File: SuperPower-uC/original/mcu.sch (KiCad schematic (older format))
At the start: 41 parts, among them J4 mcu_pinout, J5 mcu_pinout, Q5 S8050, Q6 S8050, U4 CP2102N-A01-GQFN28, U5 ESP32-WROOM32

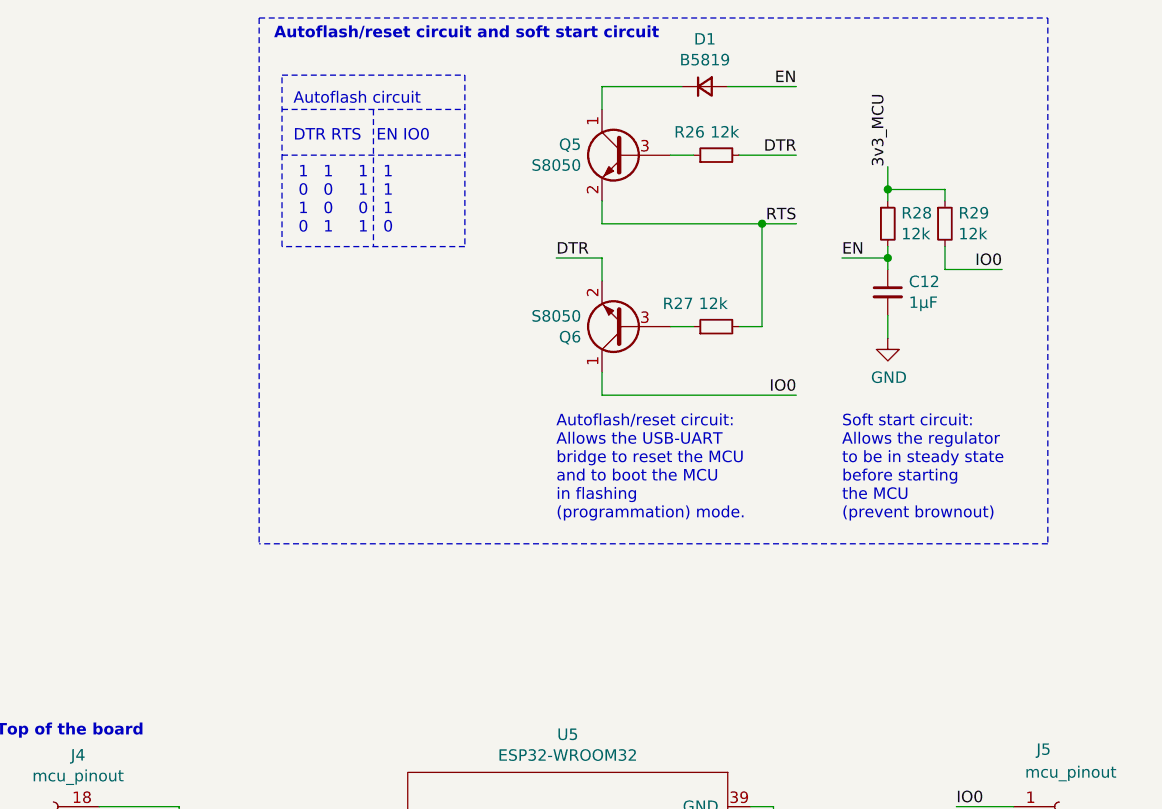
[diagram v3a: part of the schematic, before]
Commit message: Cleanup auto-reset circuit
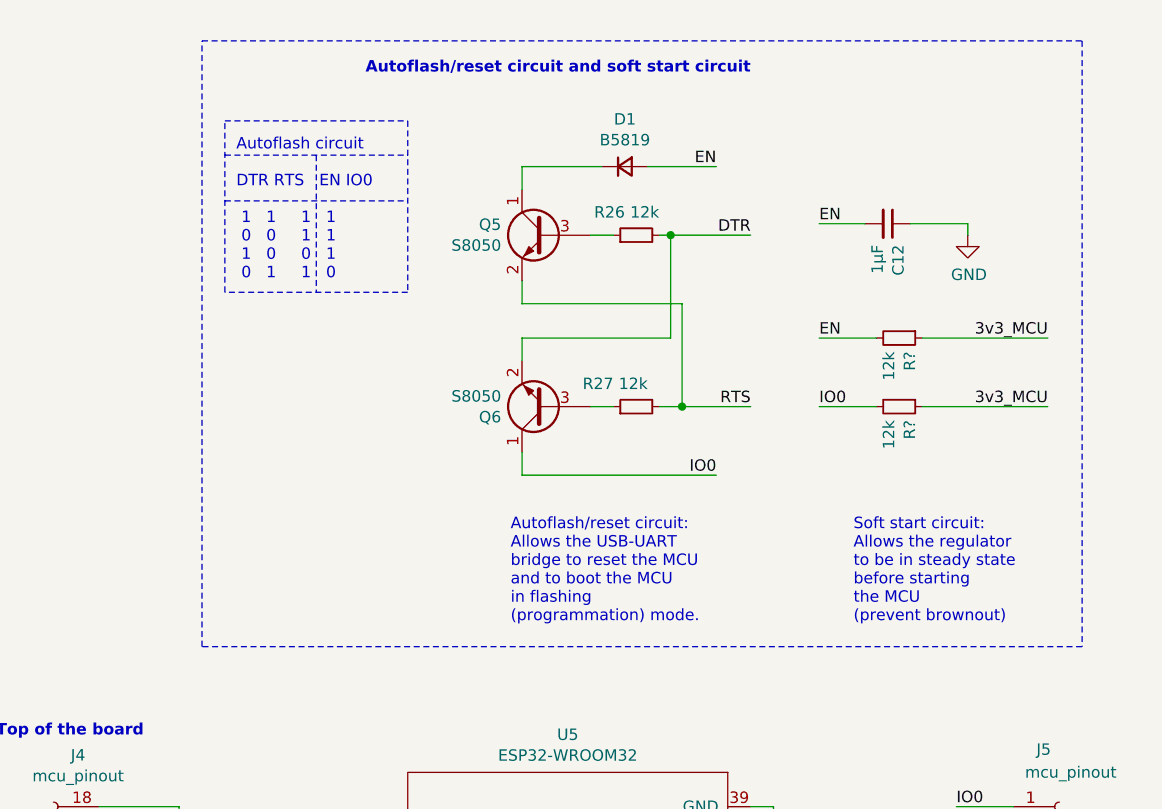
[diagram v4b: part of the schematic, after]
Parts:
- removed R28, R29: 12k, Resistor_SMD:R_0603_1608Metric, symbol Device:R_Small
- added R? (x2): 12k, Resistor_SMD:R_0603_1608Metric, symbol Device:R_Small
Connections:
- net 3v3_MCU: now also R?.1, R?.1
- net EN: now also C12.2, R?.2; no longer C12.1
- net GND: now also C12.1; no longer C12.2
- net IO0: now also R?.2
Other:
- moved on the sheet: C12, D1, Q5, Q6, R26, R27
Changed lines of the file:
@@
 	9250 5500 9500 5500
-$Comp
-L Device:R_Small R28
-U 1 1 5F8C7F33
-P 9850 1550
-F 0 "R28" H 9909 1596 50  0000 L CNN
-F 1 "12k" H 9909 1505 50  0000 L CNN
-F 2 "Resistor_SMD:R_0603_1608Metric" H 9850 1550 50  0001 C CNN
-F 3 "~" H 9850 1550 50  0001 C CNN
-	1    9850 1550
-	1    0    0    -1
-$EndComp
-$Comp
-L Device:C_Small C12
-U 1 1 5F8C82E0
-P 9850 1850
-F 0 "C12" H 9942 1896 50  0000 L CNN
-F 1 "1µF" H 9942 1805 50  0000 L CNN
-F 2 "Capacitor_SMD:C_0603_1608Metric" H 9850 1850 50  0001 C CNN
-F 3 "~" H 9850 1850 50  0001 C CNN
-	1    9850 1850
-	1    0    0    -1
-$EndComp
-Wire Wire Line
-	9850 1650 9850 1700
-Wire Wire Line
-	9650 1700 9850 1700
-Connection ~ 9850 1700
-Wire Wire Line
-	9850 1700 9850 1750
-Text Label 9650 1700 0    50   ~ 0
-EN
-$Comp
-L power:GND #PWR034
-U 1 1 5F8CBC56
-P 9850 2050
-F 0 "#PWR034" H 9850 1800 50  0001 C CNN
-F 1 "GND" H 9855 1877 50  0000 C CNN
-F 2 "" H 9850 2050 50  0001 C CNN
-F 3 "" H 9850 2050 50  0001 C CNN
-	1    9850 2050
-	1    0    0    -1
-$EndComp
-Wire Wire Line
-	9850 2050 9850 1950
-$Comp
-L Device:R_Small R29
-U 1 1 5F8CDA06
-P 10100 1550
-F 0 "R29" H 10159 1596 50  0000 L CNN
-F 1 "12k" H 10159 1505 50  0000 L CNN
-F 2 "Resistor_SMD:R_0603_1608Metric" H 10100 1550 50  0001 C CNN
-F 3 "~" H 10100 1550 50  0001 C CNN
-	1    10100 1550
-	1    0    0    -1
-$EndComp
-Wire Wire Line
-	10100 1650 10100 1750
-Wire Wire Line
-	10100 1750 10350 1750
-Text Label 10350 1750 2    50   ~ 0
-IO0
-Wire Wire Line
-	9850 1450 9850 1400
-Wire Wire Line
-	9850 1400 10100 1400
-Wire Wire Line
-	10100 1400 10100 1450
-Wire Wire Line
-	9850 1400 9850 1300
-Connection ~ 9850 1400
 $Comp
 L Device:R_Small R27
 U 1 1 5F8DFE5B
-P 9100 2000
-F 0 "R27" V 9200 2100 50  0000 L CNN
-F 1 "12k" V 9200 1950 50  0000 L CNN
-F 2 "Resistor_SMD:R_0603_1608Metric" H 9100 2000 50  0001 C CNN
-F 3 "~" H 9100 2000 50  0001 C CNN
-	1    9100 2000
+P 8750 2350
+F 0 "R27" V 8850 2450 50  0000 L CNN
+F 1 "12k" V 8850 2300 50  0000 L CNN
+F 2 "Resistor_SMD:R_0603_1608Metric" H 8750 2350 50  0001 C CNN
+F 3 "~" H 8750 2350 50  0001 C CNN
+	1    8750 2350
 	0    -1   -1   0
 $EndComp
@@
 L Device:Q_NPN_CEB Q6
 U 1 1 5F8E617A
-P 8700 2000
-F 0 "Q6" H 8891 2046 50  0000 L CNN
-F 1 "S8050" H 8891 1955 50  0000 L CNN
-F 2 "Package_TO_SOT_SMD:SOT-23" H 8900 2100 50  0001 C CNN
-F 3 "~" H 8700 2000 50  0001 C CNN
-	1    8700 2000
+P 8350 2350
+F 0 "Q6" H 8541 2396 50  0000 L CNN
+F 1 "S8050" H 8541 2305 50  0000 L CNN
+F 2 "Package_TO_SOT_SMD:SOT-23" H 8550 2450 50  0001 C CNN
+F 3 "~" H 8350 2350 50  0001 C CNN
+	1    8350 2350
 	-1   0    0    1
 $EndComp
 Wire Wire Line
-	8900 2000 9000 2000
-Wire Wire Line
-	9300 1550 9300 2000
-Wire Wire Line
-	9300 2000 9200 2000
-Wire Wire Line
-	8600 2200 8600 2300
-Text Label 9450 2300 2    50   ~ 0
-IO0
-Text Label 9450 950  2    50   ~ 0
-EN
-Wire Wire Line
-	9200 1250 9450 1250
-Text Label 9450 1250 2    50   ~ 0
+	8550 2350 8650 2350
+Wire Wire Line
+	8950 1900 8950 2350
+Wire Wire Line
+	8950 2350 8850 2350
+Wire Wire Line
+	8250 2550 8250 2650
+Text Label 9250 1600 2    50   ~ 0
 DTR
-Text Label 9450 1550 2    50   ~ 0
+Text Label 9250 2350 2    50   ~ 0
 RTS
 Wire Wire Line
-	8600 1800 8600 1700
-Wire Wire Line
-	8600 1700 8400 1700
-Text Label 8400 1700 0    50   ~ 0
-DTR
-Wire Wire Line
-	9300 1550 9450 1550
-Text Notes 7250 1600 0    50   ~ 0
+	8250 2150 8250 2050
+Text Notes 7000 1800 0    50   ~ 0
 Autoflash circuit\n\nDTR RTS   EN IO0\n\n 1   1     1   1\n 0   0     1   1\n 1   0     0   1\n 0   1     1   0
 Wire Notes Line
-	7200 900  8000 900
-Wire Notes Line
-	8000 1650 7200 1650
-Wire Notes Line
-	7200 1650 7200 900
-Wire Notes Line
-	7600 1050 7600 1650
-Text Notes 8850 750  2    50   ~ 10
+	6950 1100 7750 1100
+Wire Notes Line
+	7750 1850 6950 1850
+Wire Notes Line
+	6950 1850 6950 1100
+Wire Notes Line
+	7350 1250 7350 1850
+Text Notes 9250 900  2    50   ~ 10
 Autoflash/reset circuit and soft start circuit
 Wire Notes Line
-	7100 650  10550 650
-Wire Notes Line
-	10550 2950 7100 2950
-Connection ~ 9300 1550
-Wire Notes Line
-	7200 1250 8000 1250
-Wire Notes Line
-	7200 1050 8000 1050
-Wire Notes Line
-	8000 900  8000 1650
-Wire Wire Line
-	8600 1550 9300 1550
-Wire Wire Line
-	8600 950  8950 950
-Wire Wire Line
-	8600 1050 8600 950
-Wire Wire Line
-	8600 1450 8600 1550
-Wire Wire Line
-	8900 1250 9000 1250
+	6950 1450 7750 1450
+Wire Notes Line
+	6950 1250 7750 1250
+Wire Notes Line
+	7750 1100 7750 1850
+Wire Wire Line
+	8250 1900 8950 1900
+Wire Wire Line
+	8250 1300 8600 1300
+Wire Wire Line
+	8250 1400 8250 1300
+Wire Wire Line
+	8250 1800 8250 1900
+Wire Wire Line
+	8550 1600 8650 1600
 $Comp
 L Device:Q_NPN_CEB Q5
 U 1 1 5F8E1EE6
-P 8700 1250
-F 0 "Q5" H 8891 1296 50  0000 L CNN
-F 1 "S8050" H 8891 1205 50  0000 L CNN
-F 2 "Package_TO_SOT_SMD:SOT-23" H 8900 1350 50  0001 C CNN
-F 3 "~" H 8700 1250 50  0001 C CNN
-	1    8700 1250
+P 8350 1600
+F 0 "Q5" H 8541 1646 50  0000 L CNN
+F 1 "S8050" H 8541 1555 50  0000 L CNN
+F 2 "Package_TO_SOT_SMD:SOT-23" H 8550 1700 50  0001 C CNN
+F 3 "~" H 8350 1600 50  0001 C CNN
+	1    8350 1600
 	-1   0    0    -1
 $EndComp
@@
 L Device:R_Small R26
 U 1 1 5F8DFE61
-P 9100 1250
-F 0 "R26" V 9200 1300 50  0000 L CNN
-F 1 "12k" V 9200 1150 50  0000 L CNN
-F 2 "Resistor_SMD:R_0603_1608Metric" H 9100 1250 50  0001 C CNN
-F 3 "~" H 9100 1250 50  0001 C CNN
-	1    9100 1250
+P 8750 1600
+F 0 "R26" V 8850 1650 50  0000 L CNN
+F 1 "12k" V 8850 1500 50  0000 L CNN
+F 2 "Resistor_SMD:R_0603_1608Metric" H 8750 1600 50  0001 C CNN
+F 3 "~" H 8750 1600 50  0001 C CNN
+	1    8750 1600
 	0    -1   -1   0
 $EndComp
@@
 Text Label 9500 4700 2    50   ~ 0
 SDA
-Text Label 9850 1300 1    50   ~ 0
-3v3_MCU
 Text Label 5500 2800 2    50   ~ 0
 TXT
@@
 Text Notes 2500 6150 0    50   ~ 0
 Indicator LEDs showing\nthe serial bus status.\nAn RSTb pull-up resistor
-Text Notes 9650 2850 0    50   ~ 0
+Text Notes 9700 3300 0    50   ~ 0
 Soft start circuit:\nAllows the regulator\nto be in steady state\nbefore starting\nthe MCU\n(prevent brownout)
-Text Notes 8400 2850 0    50   ~ 0
-Autoflash/reset circuit:\nAllows the USB-UART\nbridge to reset the MCU\nand to boot the MCU\nin flashing\n(programmation) mode.
 Text Notes 3000 4350 0    50   ~ 0
 USB - UART bridge:\nAllows the MCU to communicate and to be flashed\n(programmed) via the USB bus
@@
 L Device:D_Small D1
 U 1 1 5FDAA563
-P 9050 950
-F 0 "D1" H 9050 743 50  0000 C CNN
-F 1 "B5819" H 9050 834 50  0000 C CNN
-F 2 "" V 9050 950 50  0001 C CNN
-F 3 "~" V 9050 950 50  0001 C CNN
-	1    9050 950
+P 8700 1300
+F 0 "D1" H 8700 1093 50  0000 C CNN
+F 1 "B5819" H 8700 1184 50  0000 C CNN
+F 2 "" V 8700 1300 50  0001 C CNN
+F 3 "~" V 8700 1300 50  0001 C CNN
+	1    8700 1300
 	1    0    0    1
 $EndComp
 Wire Wire Line
-	8600 2300 9450 2300
-Wire Wire Line
-	9150 950  9450 950
-Wire Notes Line
-	10550 650  10550 2950
-Wire Notes Line
-	7100 650  7100 2950
+	8850 1600 8900 1600
+Wire Wire Line
+	8900 1600 8900 2050
+Wire Wire Line
+	8900 2050 8250 2050
+Connection ~ 8900 1600
+Wire Wire Line
+	8900 1600 9250 1600
+Wire Wire Line
+	9250 2350 8950 2350
+Connection ~ 8950 2350
+Wire Wire Line
+	8800 1300 9100 1300
+Text Label 9100 1300 2    50   ~ 0
+EN
+Wire Wire Line
+	8250 2650 9100 2650
+Text Label 9100 2650 2    50   ~ 0
+IO0
+$Comp
+L power:GND #PWR034
+U 1 1 5F8CBC56
+P 10200 1600
+F 0 "#PWR034" H 10200 1350 50  0001 C CNN
+F 1 "GND" H 10205 1427 50  0000 C CNN
+F 2 "" H 10200 1600 50  0001 C CNN
+F 3 "" H 10200 1600 50  0001 C CNN
+	1    10200 1600
+	1    0    0    -1
+$EndComp
+Text Label 9550 1550 0    50   ~ 0
+EN
+Wire Wire Line
+	9550 1550 9750 1550
+$Comp
+L Device:C_Small C12
+U 1 1 5F8C82E0
+P 9850 1550
+F 0 "C12" H 9942 1596 50  0000 L CNN
+F 1 "1µF" H 9942 1505 50  0000 L CNN
+F 2 "Capacitor_SMD:C_0603_1608Metric" H 9850 1550 50  0001 C CNN
+F 3 "~" H 9850 1550 50  0001 C CNN
+	1    9850 1550
+	0    1    1    0
+$EndComp
+Text Label 9550 2050 0    50   ~ 0
+EN
+$Comp
+L Device:R_Small R?
+U 1 1 5FE5C5F7
+P 9900 2050
+F 0 "R?" H 9959 2096 50  0000 L CNN
+F 1 "12k" H 9959 2005 50  0000 L CNN
+F 2 "Resistor_SMD:R_0603_1608Metric" H 9900 2050 50  0001 C CNN
+F 3 "~" H 9900 2050 50  0001 C CNN
+	1    9900 2050
+	0    1    1    0
+$EndComp
+Text Label 10550 2050 2    50   ~ 0
+3v3_MCU
+Wire Wire Line
+	9550 2050 9800 2050
+Wire Wire Line
+	10000 2050 10550 2050
+$Comp
+L Device:R_Small R?
+U 1 1 5FE7288F
+P 9900 2350
+F 0 "R?" H 9959 2396 50  0000 L CNN
+F 1 "12k" H 9959 2305 50  0000 L CNN
+F 2 "Resistor_SMD:R_0603_1608Metric" H 9900 2350 50  0001 C CNN
+F 3 "~" H 9900 2350 50  0001 C CNN
+	1    9900 2350
+	0    1    1    0
+$EndComp
+Text Label 10550 2350 2    50   ~ 0
+3v3_MCU
+Wire Wire Line
+	9550 2350 9800 2350
+Wire Wire Line
+	10000 2350 10550 2350
+Text Label 9550 2350 0    50   ~ 0
+IO0
+Wire Wire Line
+	10200 1600 10200 1550
+Wire Wire Line
+	10200 1550 9950 1550
+Text Notes 8200 3300 0    50   ~ 0
+Autoflash/reset circuit:\nAllows the USB-UART\nbridge to reset the MCU\nand to boot the MCU\nin flashing\n(programmation) mode.
+Wire Notes Line
+	6850 750  10700 750
+Wire Notes Line
+	10700 750  10700 3400
+Wire Notes Line
+	10700 3400 6850 3400
+Wire Notes Line
+	6850 3400 6850 750
 $EndSCHEMATC

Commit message: Re-Annotate project
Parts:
- D4: renamed from D1; value B5819 -> B5819W; footprint (none) -> Diode_SMD:D_SOD-123
- gave numbers to parts that had none: 2
- renumbered C9 to C10, C10 to C11, C11 to C12, C12 to C13, C21 to C9, D6 to D3, J4 to J7, J5 to J8, Q5 to Q7, Q6 to Q8, R19 to R27, R22 to R28, R20 to R29, R21 to R30, R5 to R31, R23 to R32, R24 to R33, R25 to R34, R26 to R35, R27 to R36, TP9 to TP18, TP10 to TP19, TP11 to TP20, TP12 to TP21, TP13 to TP22, TP14 to TP23, TP4 to TP24, TP5 to TP25, TP6 to TP26, TP7 to TP27, TP8 to TP28, TP1 to TP29, TP2 to TP30, TP3 to TP31, U4 to U6, U5 to U7

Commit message: Add 3D file to every component
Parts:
- D3: footprint LED_SMD:LED_SK6812MINI_PLCC4_3.5x3.5mm_P1.75mm -> LED_SMD:LED_SK6812_PLCC4_5.0x5.0mm_P3.2mm
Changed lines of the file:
@@
 F 0 "D3" H 2044 7046 50  0000 L CNN
 F 1 "SK6812" H 2044 6955 50  0000 L CNN
-F 2 "LED_SMD:LED_SK6812MINI_PLCC4_3.5x3.5mm_P1.75mm" H 1750 6700 50  0001 L TNN
+F 2 "LED_SMD:LED_SK6812_PLCC4_5.0x5.0mm_P3.2mm" H 1750 6700 50  0001 L TNN
 F 3 "https://cdn-shop.adafruit.com/product-files/1138/SK6812+LED+datasheet+.pdf" H 1800 6625 50  0001 L TNN
 	1    1700 7000

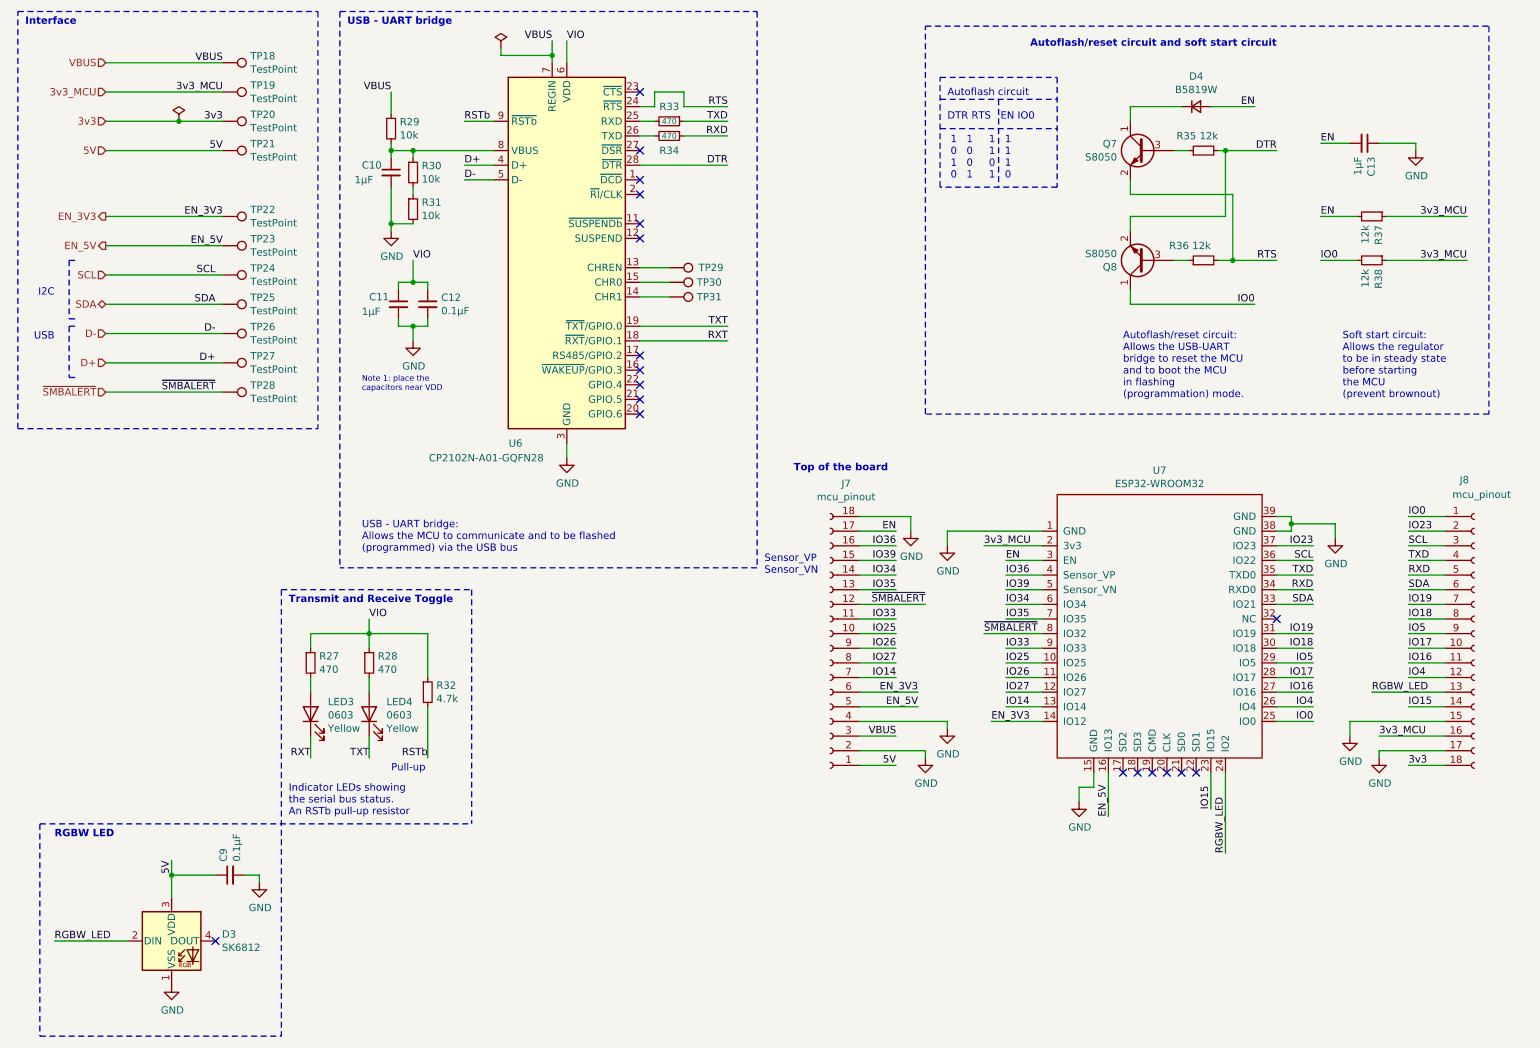
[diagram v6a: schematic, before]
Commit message: Layed out IO sheet parts
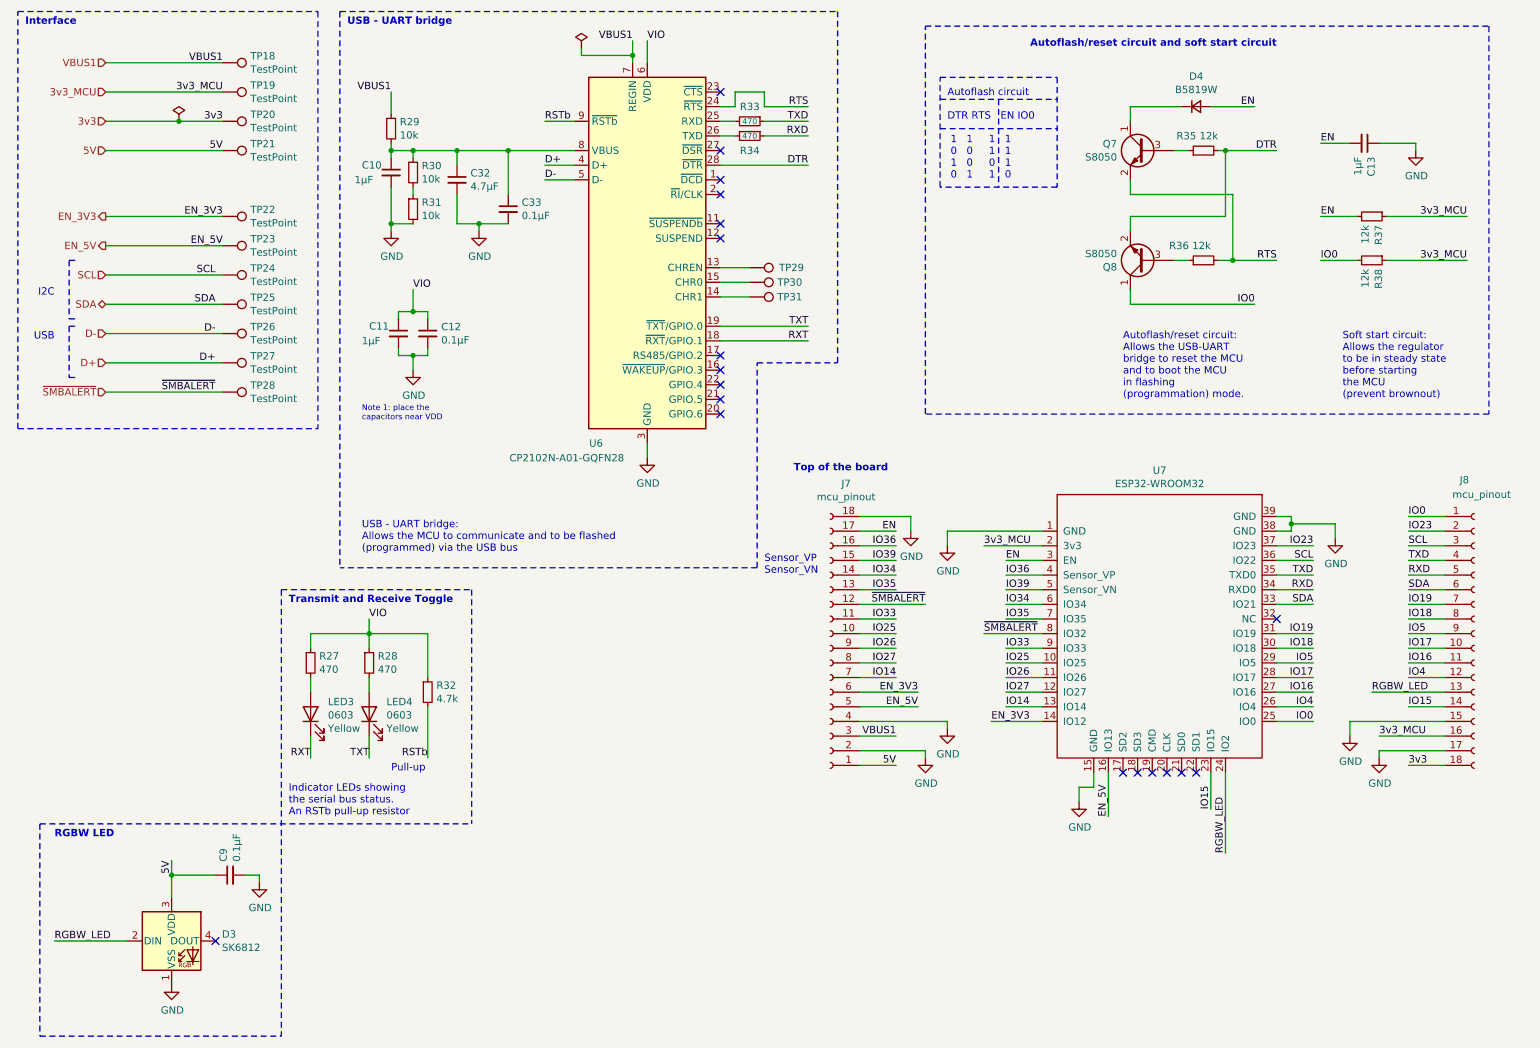
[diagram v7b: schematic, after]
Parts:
- added C32: 4.7µF, Capacitor_SMD:C_0603_1608Metric, symbol Device:C_Small
- added C33: 0.1µF, Capacitor_SMD:C_0603_1608Metric, symbol Device:C_Small
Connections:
- net GND: now also C32.2, C33.2
- net at C10.1, R29.2, R30.1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: now also C32.1, C33.1
- net VBUS renamed VBUS1
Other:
- moved on the sheet: C11, C12, R33, R34, TP29, TP30, TP31, U6
